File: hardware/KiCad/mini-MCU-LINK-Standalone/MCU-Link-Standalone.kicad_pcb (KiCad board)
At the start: 2 copper layers, 46 x 19 mm, 69 parts, among them J1 USB4110-GF-A_REVB, J2 BM03B-SRSS-TB, J3 Conn_02x05_Odd_Even, Q1 PMDXB290UNE, Q2 PMDXB290UNE, Q3 PMDXB290UNE, SW1 KMR221GLFS, U1 XC6227C331PR-G, U2 LPC55S69JBD64, U3 STMPS2141STR, Y1 16.000MHz

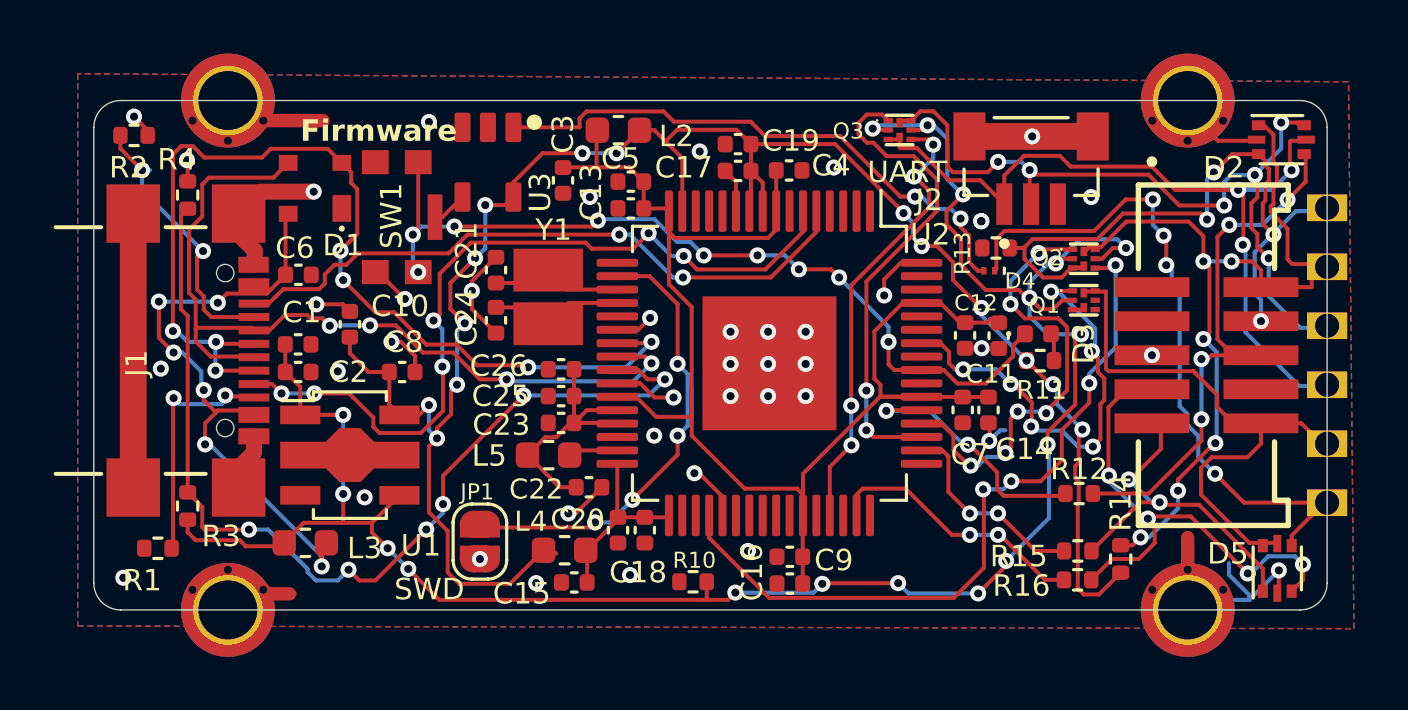
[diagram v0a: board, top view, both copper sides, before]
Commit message: fixed some DRC errors and warnings
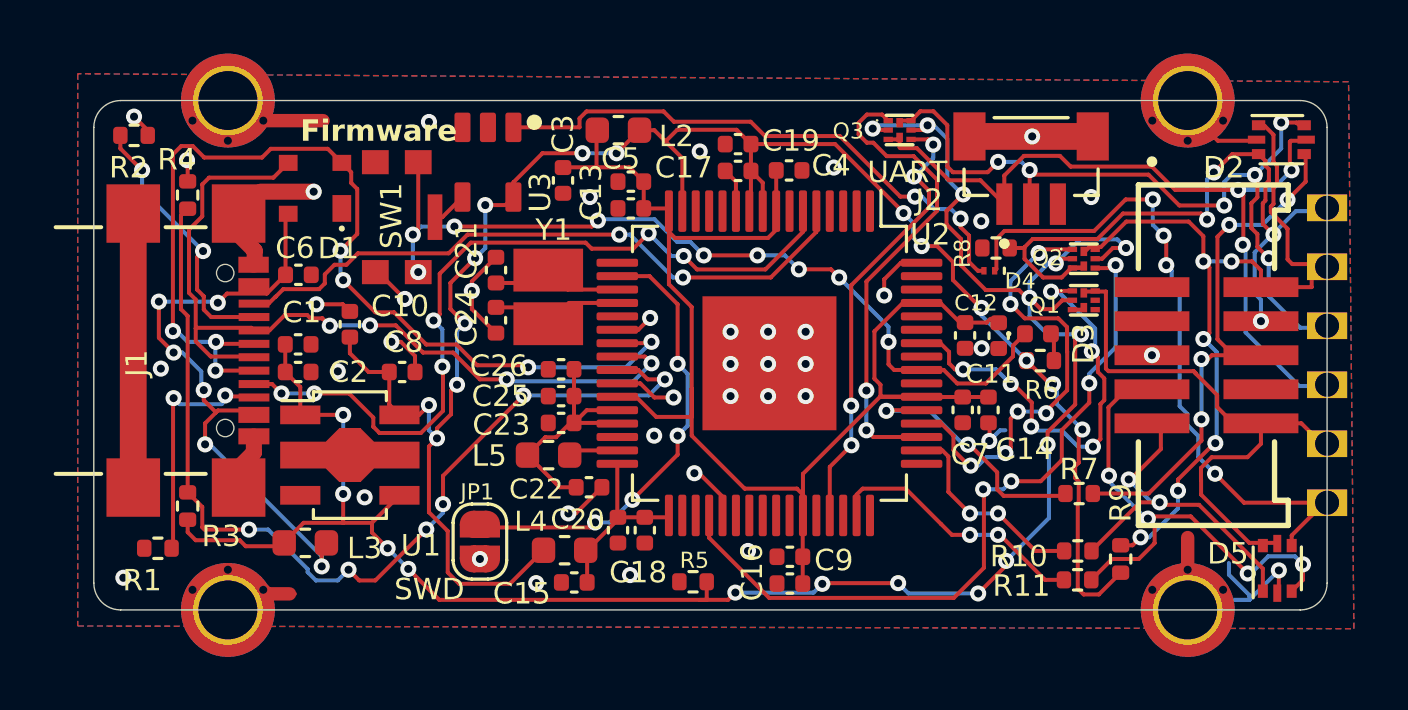
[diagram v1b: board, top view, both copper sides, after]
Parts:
- renumbered R15 to R10, R16 to R11, R10 to R5, R11 to R6, R12 to R7, R13 to R8, R14 to R9
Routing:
- net GND: vias 42 -> 41
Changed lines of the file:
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@@
     (property "ki_description" "Jumper, 2-pole, closed/bridged")
     (property "ki_keywords" "Jumper SPST")
-    (attr exclude_from_pos_files exclude_from_bom)
+    (attr exclude_from_pos_files)
     (fp_text reference "JP1" (at -1.85 0.1) (layer "F.SilkS")
         (effects (font (size 0.6 0.6) (thickness 0.15)))
@@
     (property "ki_keywords" "R res resistor")
     (attr smd)
-    (fp_text reference "R12" (at 0.000781 0.908112 unlocked) (layer "F.SilkS")
+    (fp_text reference "R7" (at 0.000781 0.908112 unlocked) (layer "F.SilkS")
         (effects (font (size 0.8 0.8) (thickness 0.15)))
     )
@@
     (property "ki_keywords" "ESD protection diode")
     (attr through_hole)
-    (fp_text reference "D1" (at -2.125 1.05 unlocked) (layer "F.SilkS")
+    (fp_text reference "D1" (at -2.2376 0.8686 unlocked) (layer "F.SilkS")
         (effects (font (size 0.8 0.8) (thickness 0.15)))
     )
@@
     (property "ki_keywords" "R res resistor")
     (attr smd)
-    (fp_text reference "R13" (at 1.25 -0.2 90 unlocked) (layer "F.SilkS")
+    (fp_text reference "R8" (at 1.25 -0.2 90 unlocked) (layer "F.SilkS")
         (effects (font (size 0.6 0.6) (thickness 0.15)))
     )
@@
     (property "ki_keywords" "R res resistor")
     (attr smd)
-    (fp_text reference "R11" (at 0.05 1.1 unlocked) (layer "F.SilkS")
+    (fp_text reference "R6" (at 0.05 1.1 unlocked) (layer "F.SilkS")
         (effects (font (size 0.7 0.7) (thickness 0.15)))
     )
@@
     (property "ki_keywords" "R res resistor")
     (attr smd)
-    (fp_text reference "R10" (at -0.05 0.8) (layer "F.SilkS")
+    (fp_text reference "R5" (at -0.05 0.8) (layer "F.SilkS")
         (effects (font (size 0.6 0.6) (thickness 0.15)))
     )
@@
     (property "ki_keywords" "R res resistor")
     (attr smd)
-    (fp_text reference "R14" (at 2.1 0 90 unlocked) (layer "F.SilkS")
+    (fp_text reference "R9" (at 2.1 0 90 unlocked) (layer "F.SilkS")
         (effects (font (size 0.8 0.8) (thickness 0.15)))
     )
@@
     (property "ki_keywords" "R res resistor")
     (attr smd)
-    (fp_text reference "R16" (at -2.094307 0.222073 unlocked) (layer "F.SilkS")
+    (fp_text reference "R11" (at -2.094307 0.222073 unlocked) (layer "F.SilkS")
         (effects (font (size 0.8 0.8) (thickness 0.15)))
     )
@@
     (property "ki_keywords" "R res resistor")
     (attr smd)
-    (fp_text reference "R15" (at -2.201796 0.200561 unlocked) (layer "F.SilkS")
+    (fp_text reference "R10" (at -2.201796 0.200561 unlocked) (layer "F.SilkS")
         (effects (font (size 0.8 0.8) (thickness 0.15)))
     )
@@
   (segment (start 167.345 67.145) (end 167.345 66.162588) (width 0.15) (layer "F.Cu") (net 1))
   (segment (start 171.6 70.236619) (end 171.605 70.241619) (width 0.15) (layer "F.Cu") (net 1))
-  (segment (start 157.85 79.625) (end 157.95 79.625) (width 0.15) (layer "F.Cu") (net 1))
   (segment (start 167.345 66.162588) (end 166.803811 65.621399) (width 0.15) (layer "F.Cu") (net 1))
   (segment (start 145.375 76.75) (end 145.375 77.115) (width 0.15) (layer "F.Cu") (net 1))
@@
   (via (at 161.55 72.025) (size 0.6) (drill 0.3) (layers "F.Cu" "B.Cu") (net 2))
   (via (at 160.15 70.825) (size 0.6) (drill 0.3) (layers "F.Cu" "B.Cu") (net 2))
-  (via (at 168.1 65.5) (size 0.6) (drill 0.3) (layers "F.Cu" "B.Cu") (free) (net 2))
   (via (at 151.5 79) (size 0.6) (drill 0.3) (layers "F.Cu" "B.Cu") (free) (net 2))
   (via (at 170 62.338967) (size 0.6) (drill 0.3) (layers "F.Cu" "B.Cu") (free) (net 2))
@@
   (segment (start 155.974264 72.8) (end 155.224264 72.05) (width 0.15) (layer "F.Cu") (net 3))
   (segment (start 164.325707 72.05) (end 164.341622 72.034085) (width 0.15) (layer "F.Cu") (net 3))
-  (segment (start 160.44789 63.601499) (end 160.45255 63.606159) (width 0.15) (layer "F.Cu") (net 3))
   (segment (start 157.3 71.75) (end 157.3 72.8) (width 0.15) (layer "F.Cu") (net 3))
   (segment (start 155.51 65.025) (end 155.51 64.025) (width 0.15) (layer "F.Cu") (net 3))
@@
   (segment (start 148.322792 71.8245) (end 148.322792 72.701472) (width 0.15) (layer "F.Cu") (net 5))
   (segment (start 171.735781 75.992229) (end 171.7 76.02801) (width 0.15) (layer "F.Cu") (net 5))
-  (segment (start 173.2 78.71) (end 173.3 78.61) (width 0.15) (layer "F.Cu") (net 5))
   (segment (start 171.7 79.202737) (end 171.92019 79.422927) (width 0.15) (layer "F.Cu") (net 5))
   (segment (start 171.7 76.02801) (end 171.7 79.202737) (width 0.15) (layer "F.Cu") (net 5))
@@
   (segment (start 172.488424 79.422927) (end 173.3 78.611351) (width 0.15) (layer "F.Cu") (net 5))
   (segment (start 165.200417 65.176153) (end 162.649264 62.625) (width 0.15) (layer "F.Cu") (net 5))
-  (segment (start 152.25 77.9) (end 152.2025 77.8525) (width 0.15) (layer "F.Cu") (net 5))
   (segment (start 148.3 68.775217) (end 148.834274 69.309491) (width 0.15) (layer "F.Cu") (net 5))
   (segment (start 167.045 67.020736) (end 166.453506 66.429242) (width 0.15) (layer "F.Cu") (net 5))
@@
   (segment (start 155.8 70) (end 154.8505 70.9495) (width 0.15) (layer "B.Cu") (net 10))
   (segment (start 138.501483 70.001483) (end 138.1 69.6) (width 0.15) (layer "B.Cu") (net 10))
-  (segment (start 137.95 69.6) (end 137.95 69.625) (width 0.15) (layer "B.Cu") (net 10))
   (segment (start 138.1 69.6) (end 137.95 69.6) (width 0.15) (layer "B.Cu") (net 10))
-  (segment (start 139.397585 71.072585) (end 139.534138 71.072585) (width 0.15) (layer "B.Cu") (net 10))
   (segment (start 139.55574 70.001483) (end 139.534138 70.023085) (width 0.15) (layer "B.Cu") (net 10))
   (segment (start 144.3 67.7) (end 144.2 67.6) (width 0.15) (layer "B.Cu") (net 10))
@@
   (segment (start 155.910737 65.426518) (end 156.759219 66.275) (width 0.15) (layer "B.Cu") (net 17))
   (segment (start 152.75 74.225) (end 152.925 74.05) (width 0.15) (layer "F.Cu") (net 18))
-  (segment (start 152.75 74.05) (end 152.75 74.225) (width 0.15) (layer "F.Cu") (net 18))
   (segment (start 152.925 74.05) (end 154.525 74.05) (width 0.15) (layer "F.Cu") (net 18))
-  (segment (start 152.9625 74.4375) (end 152.75 74.225) (width 0.15) (layer "F.Cu") (net 18))
   (segment (start 167.645 66.038324) (end 167.645 67.020736) (width 0.15) (layer "F.Cu") (net 19))
   (segment (start 167.328811 65.722135) (end 167.645 66.038324) (width 0.15) (layer "F.Cu") (net 19))
@@
   (segment (start 165.699264 62.775) (end 166.899218 63.974954) (width 0.15) (layer "F.Cu") (net 23))
   (segment (start 179.61 63.536537) (end 179.61 62.54) (width 0.15) (layer "F.Cu") (net 23))
-  (segment (start 168.754375 64.658746) (end 168.959596 64.863967) (width 0.15) (layer "F.Cu") (net 23))
   (segment (start 174.463967 63.463967) (end 171.434596 63.463967) (width 0.15) (layer "F.Cu") (net 23))
   (segment (start 175.334981 64.334981) (end 174.463967 63.463967) (width 0.15) (layer "F.Cu") (net 23))
@@
   (segment (start 171.85 67.25) (end 171.925 67.175) (width 0.15) (layer "F.Cu") (net 25))
   (segment (start 178.485 63.0375) (end 178.7 63.2525) (width 0.15) (layer "F.Cu") (net 25))
-  (segment (start 178.3 63.0375) (end 178.485 63.0375) (width 0.15) (layer "F.Cu") (net 25))
   (via (at 178.5325 69.23) (size 0.6) (drill 0.3) (layers "F.Cu" "B.Cu") (net 25))
   (via (at 176.774651 63.68417) (size 0.6) (drill 0.3) (layers "F.Cu" "B.Cu") (net 25))
@@
   (via (at 139.0745 66.615) (size 0.6) (drill 0.3) (layers "F.Cu" "B.Cu") (net 57))
   (via (at 136.8 63.6) (size 0.6) (drill 0.3) (layers "F.Cu" "B.Cu") (net 57))
-  (segment (start 136.8 63.6) (end 137.1 63.6) (width 0.15) (layer "B.Cu") (net 57))
   (segment (start 139.0745 66.615) (end 136.8 64.3405) (width 0.15) (layer "B.Cu") (net 57))
   (segment (start 136.8 64.3405) (end 136.8 63.6) (width 0.15) (layer "B.Cu") (net 57))
@@
   (segment (start 137.9 77.7) (end 137.955 77.645) (width 0.15) (layer "F.Cu") (net 58))
   (segment (start 137.955 72.1205) (end 137.9755 72.1) (width 0.15) (layer "F.Cu") (net 58))
-  (segment (start 140.936873 72.036873) (end 140.975 72.075) (width 0.15) (layer "F.Cu") (net 58))
   (via (at 139.9 72) (size 0.6) (drill 0.3) (layers "F.Cu" "B.Cu") (net 58))
   (via (at 137.9755 72.1) (size 0.6) (drill 0.3) (layers "F.Cu" "B.Cu") (net 58))
@@
   (segment (start 175.2 67.8) (end 175.5 68.1) (width 0.15) (layer "B.Cu") (net 60))
   (segment (start 174.9 66.038727) (end 174.5 65.638727) (width 0.15) (layer "B.Cu") (net 60))
-  (segment (start 174.5 64.689727) (end 174.5 64.734309) (width 0.15) (layer "B.Cu") (net 60))
   (segment (start 175.5 68.1) (end 175.5 72.4) (width 0.15) (layer "B.Cu") (net 60))
   (segment (start 176.2 74.3) (end 176.820878 74.920878) (width 0.15) (layer "B.Cu") (net 60))
@@
   (segment (start 178.8 78) (end 179.8 78) (width 0.15) (layer "B.Cu") (net 63))
   (segment (start 179.8 78) (end 180.1 78.3) (width 0.15) (layer "B.Cu") (net 63))
-  (segment (start 174.4075 67.9) (end 174.4675 67.96) (width 0.15) (layer "F.Cu") (net 65))
   (segment (start 163.833723 62.572449) (end 163.526186 62.264912) (width 0.15) (layer "F.Cu") (net 66))
   (segment (start 165.575 63.075) (end 164.575 63.075) (width 0.15) (layer "F.Cu") (net 66))
